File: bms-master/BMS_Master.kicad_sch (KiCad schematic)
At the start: 88 parts, among them J1 Conn_PWR, J2 PROG, J3 Conn_Fault, J4 BMS_M_IN, J5 Conn_CAN, J6 Conn_CRSOUT, J7 Conn_CRS, J8 Micro_SD_Card, J9 USB_C_Receptacle_USB2.0_16P, Q1 SS9013, SW1 SW_SPST, U1 AP2204K-ADJ, U2 AP2204K-ADJ, U3 STM32F103C8Tx, U4 BQ79600-Q1, U5 SN65HVD256D, U6 XTR117, Y1 8M, Y2 32.768k

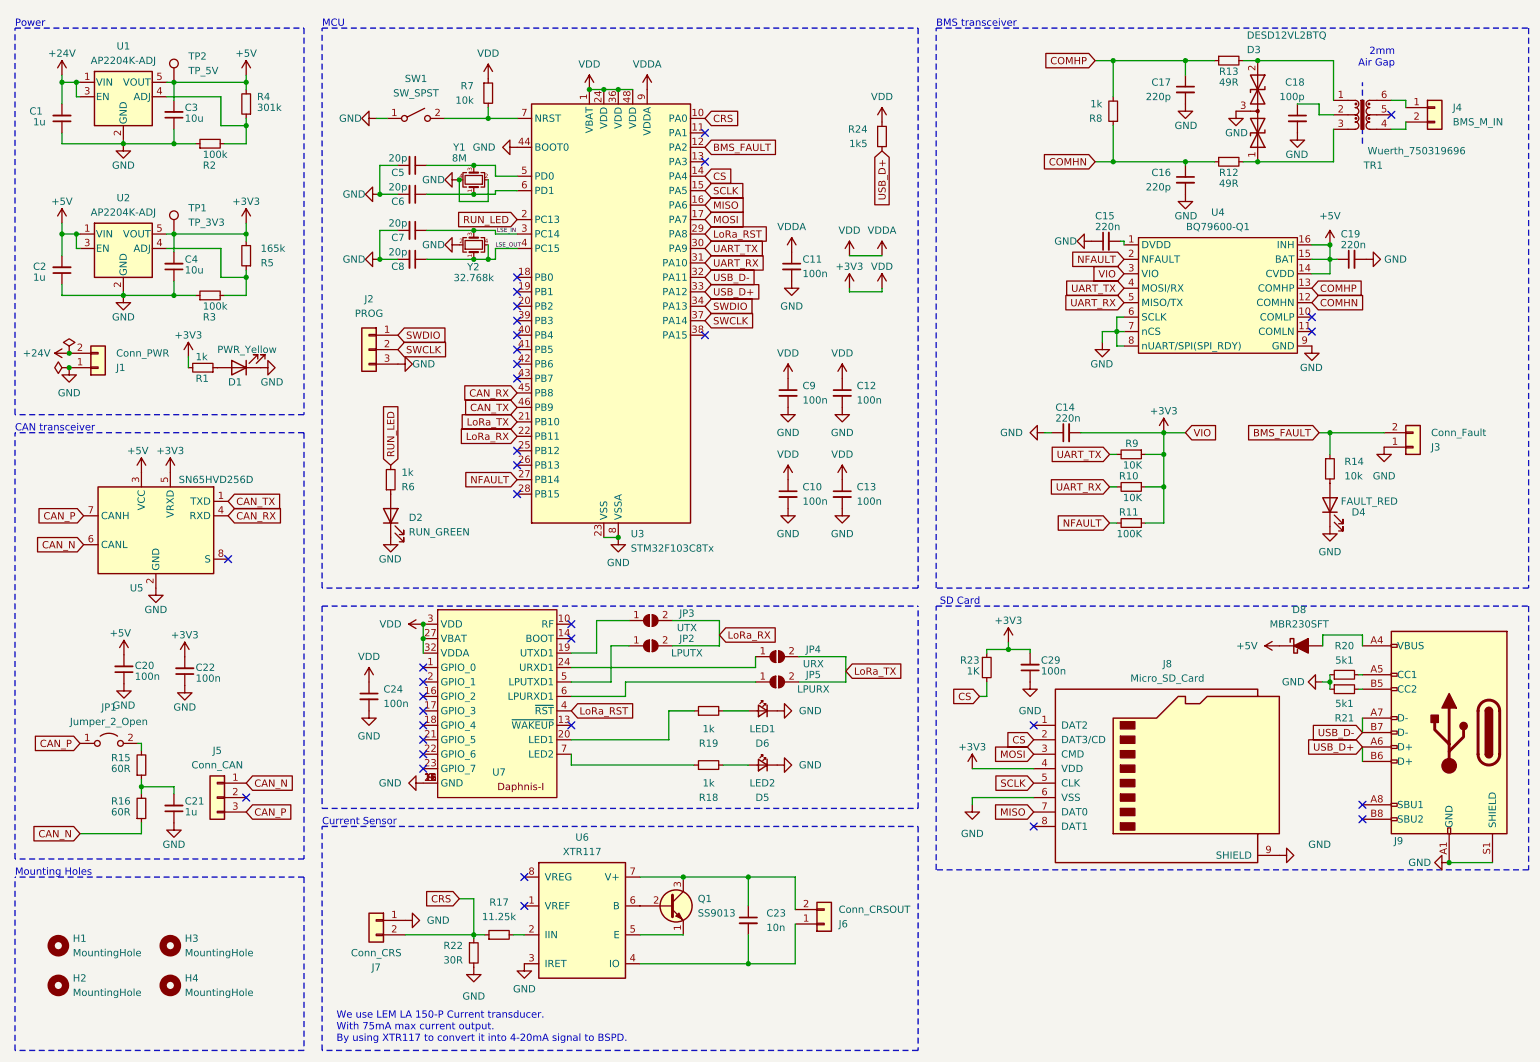
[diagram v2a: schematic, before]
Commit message: fix: CAN bus pin error
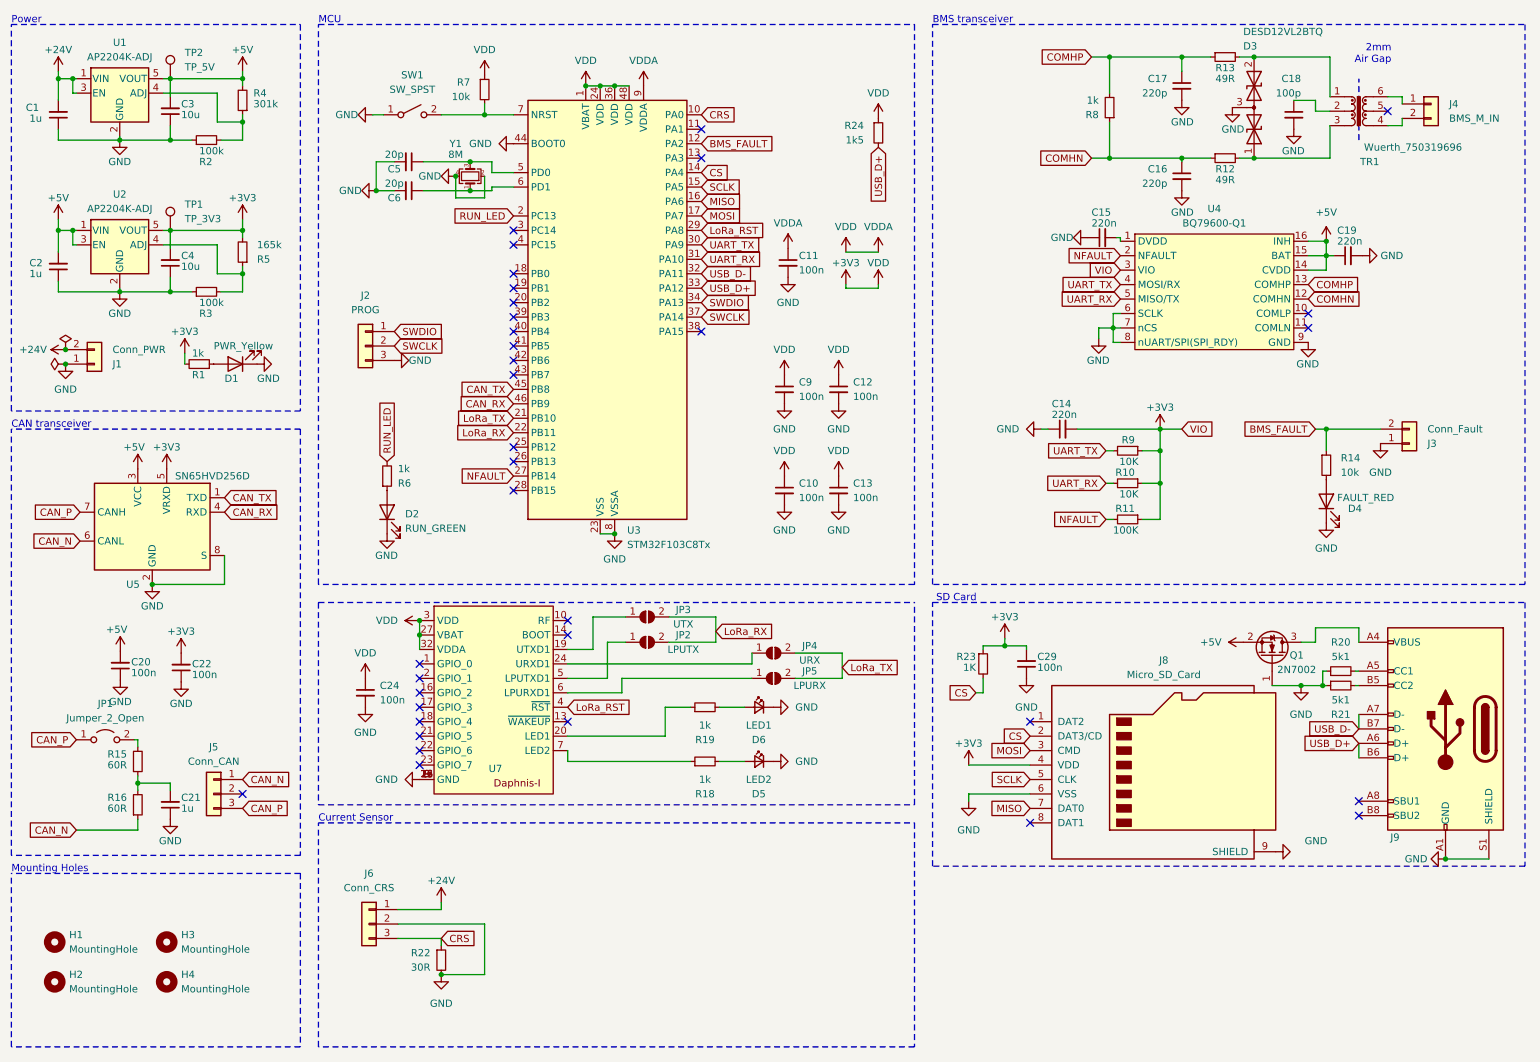
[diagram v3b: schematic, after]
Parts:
- removed C23: 10n, Capacitor_SMD:C_0603_1608Metric, symbol Device:C_Small
- removed C7, C8: 20p, Capacitor_SMD:C_0603_1608Metric, symbol Device:C_Small
- removed D8: MBR230SFT, Diode_SMD:D_SOD-123F, symbol PCM_Diode_Schottky_AKL:MBR230SFT
- removed J6: Conn_CRSOUT, Connector_JST:JST_XH_B2B-XH-A_1x02_P2.50mm_Vertical, symbol Connector_Generic:Conn_01x02
- removed J7: Conn_CRS, Connector_JST:JST_XH_B2B-XH-A_1x02_P2.50mm_Vertical, symbol Connector_Generic:Conn_01x02
- removed Q1: SS9013, Package_TO_SOT_SMD:SOT-23, symbol PCM_Transistor_BJT_AKL:SS9013
- removed R17: 11.25k, Resistor_SMD:R_0603_1608Metric, symbol Device:R_Small
- removed U6: XTR117, Package_SO:SOIC-8_3.9x4.9mm_P1.27mm, symbol Interface_CurrentLoop:XTR116U
- removed Y2: 32.768k, Crystal:Crystal_SMD_SeikoEpson_FA238-4Pin_3.2x2.5mm, symbol Device:Crystal_GND24_Small
- added J6: Conn_CRS, Connector_JST:JST_XH_B3B-XH-A_1x03_P2.50mm_Vertical, symbol Connector_Generic:Conn_01x03
- added Q1: 2N7002, Package_TO_SOT_SMD:SOT-23, symbol Transistor_FET:2N7002
- JP1: footprint PCM_Jumper_AKL:Jumper_P2.54mm_D0.7mm -> TestPoint:TestPoint_2Pads_Pitch2.54mm_Drill0.8mm
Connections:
- net +24V: now also J6.1 (Pin_1)
- net +5V: now also Q1.2 (S)
- net CAN_RX: now also U3.46 (PB9); no longer U3.45 (PB8)
- net CAN_TX: now also U3.45 (PB8); no longer U3.46 (PB9)
- net CRS: now also J6.3 (Pin_3)
- net GND: now also U5.8 (S), J6.2 (Pin_2), Q1.1 (G)
- net at J9.A4 (VBUS), J9.A9 (VBUS), J9.B4 (VBUS)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: now also Q1.3 (D)
- net LSE_IN: no longer names the net of U3.3 (PC14)
- net LSE_OUT: no longer names the net of U3.4 (PC15)
- no-connect marks 36 -> 35
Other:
- note removed: "We use LEM LA 150-P Current transducer. With 75mA max current output. By using XTR117 to convert it into 4-20mA signal to BSPD."
- moved on the sheet: C1, C10, C11, C12, C13, C14, C15, C16, C17, C18, C19, C2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

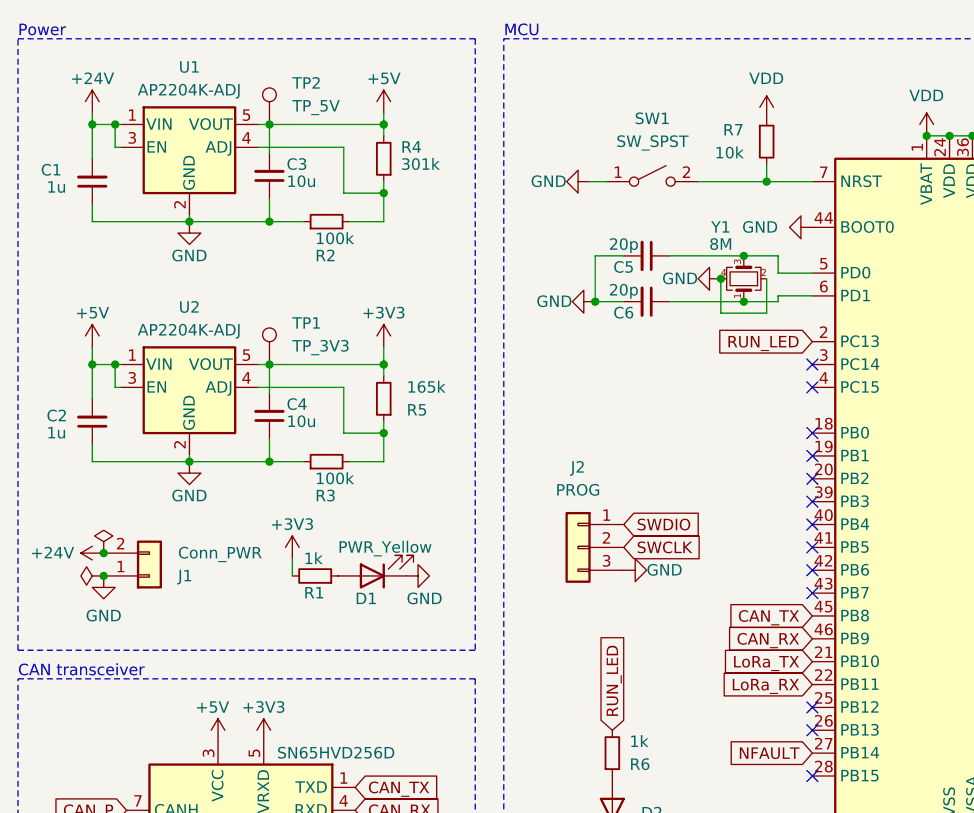
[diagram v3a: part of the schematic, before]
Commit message: feat: add DCDC and fix layout
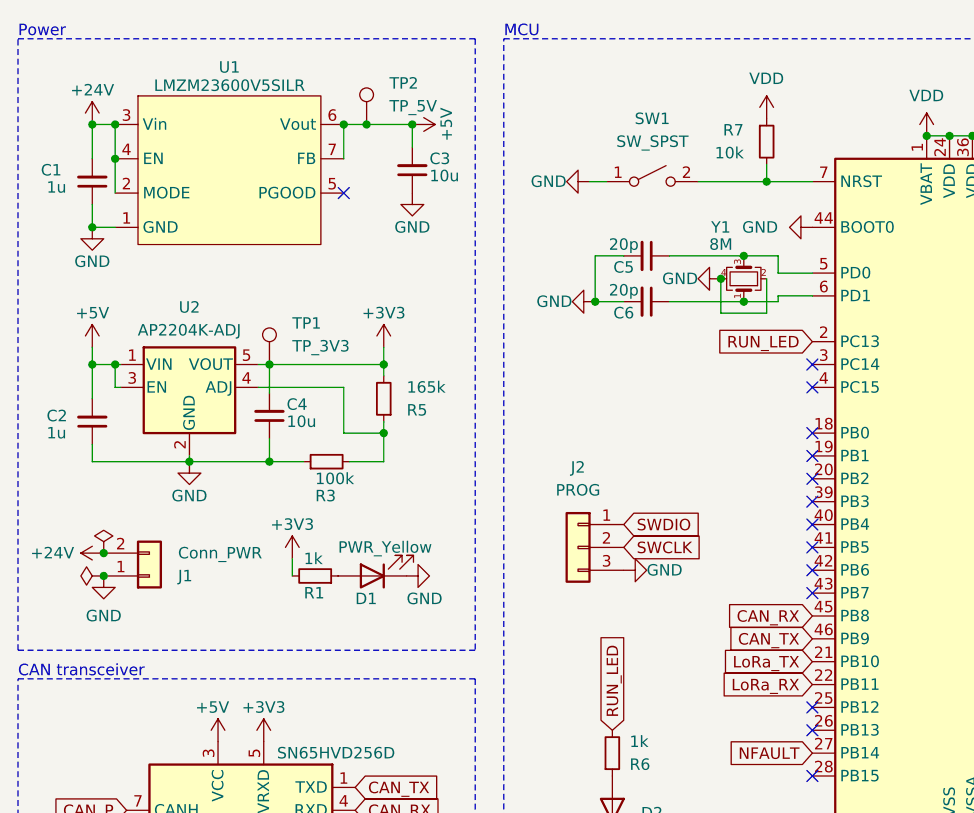
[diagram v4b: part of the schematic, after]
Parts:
- removed R2: 100k, Resistor_SMD:R_0603_1608Metric, symbol Device:R_Small
- removed R4: 301k, Resistor_SMD:R_0603_1608Metric, symbol Device:R_Small
- removed U1: AP2204K-ADJ, Package_TO_SOT_SMD:SOT-23-5, symbol Regulator_Linear:AP2204K-ADJ
- added U1: LMZM23600V5SILR, bms-master:MODULE_LMZM23601V5SILR, symbol bms-master:LMZM23600V5SILR
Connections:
- net +24V: now also U1.2 (MODE), U1.3 (Vin), U1.4 (EN)
- net +5V: now also U1.6 (Vout), U1.7 (FB)
- net CAN_RX: now also U3.45 (PB8); no longer U3.46 (PB9)
- net CAN_TX: now also U3.46 (PB9); no longer U3.45 (PB8)
- net GND: now also U1.1 (GND)
- new net: U1.10 (DNC), U1.8 (DNC), U1.9 (DNC)
- no-connect marks 35 -> 36
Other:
- moved on the sheet: C3, TP2
